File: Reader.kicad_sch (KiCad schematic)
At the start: 39 parts, among them J1 Conn_01x04, J2 Amphenol Dubox ‎76383-402LF‎, J3 Conn_01x04, J4 Conn_01x08, J5 Conn_01x10, J6 Conn_01x03, J7 Conn_01x02, Q1 2N7002, Q2 2N7002, Q3 2N7002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

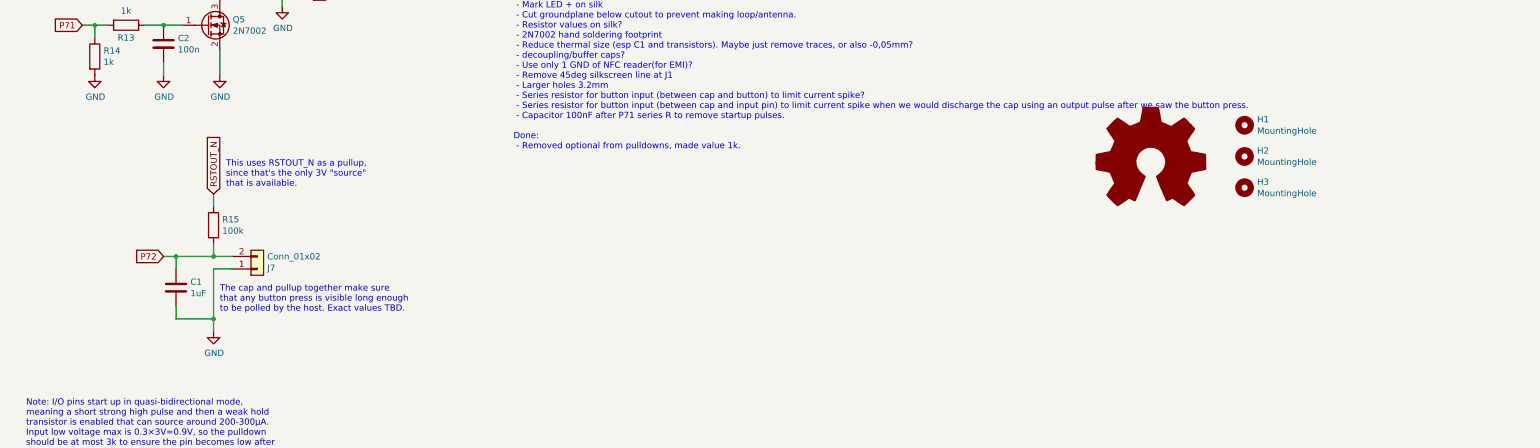
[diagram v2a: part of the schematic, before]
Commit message: Add series resistors for button input
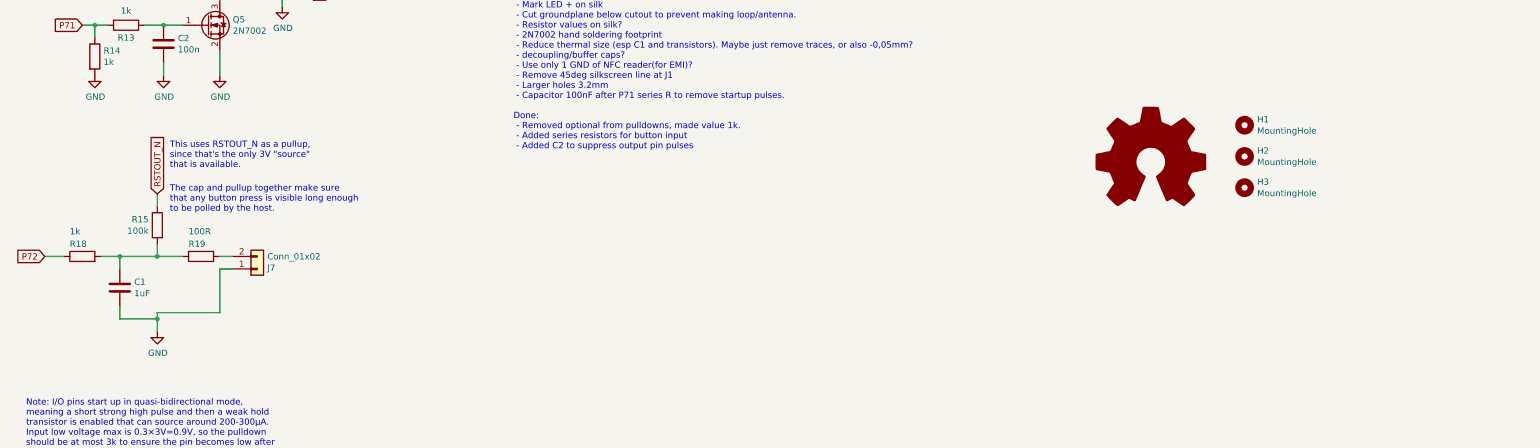
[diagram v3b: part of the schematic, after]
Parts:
- added R18: 1k, Resistor_SMD:R_0805_2012Metric_Pad1.20x1.40mm_HandSolder, symbol Device:R
- added R19: 100R, Resistor_SMD:R_0805_2012Metric_Pad1.20x1.40mm_HandSolder, symbol Device:R
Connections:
- net P72: now also R18.1; no longer C1.1, J7.2 (Pin_2), R15.2
- new net: J7.2 (Pin_2), R19.2
- new net: C1.1, R15.2, R18.2, R19.1
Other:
- note added: "TODO: - Mark LED + on silk - Cut groundplane below cutout to prevent making loop/antenna. - Resistor values on silk? - 2N7002 hand soldering footprint - Reduce thermal size (esp C1 and transistors). Maybe just remove traces, or also -0,05mm? - decoupling/buffer caps? - Use only 1 GND of NFC reader(for EMI)? - Remove 45deg silkscreen line at J1 - Larger holes 3.2mm - Capacitor 100nF after P71 seri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"
- note added: "The cap and pullup together make sure that any button press is visible long enough to be polled by the host."
- note removed: "TODO: - Mark LED + on silk - Cut groundplane below cutout to prevent making loop/antenna. - Resistor values on silk? - 2N7002 hand soldering footprint - Reduce thermal size (esp C1 and transistors). Maybe just remove traces, or also -0,05mm? - decoupling/buffer caps? - Use only 1 GND of NFC reader(for EMI)? - Remove 45deg silkscreen line at J1 - Larger holes 3.2mm - Series resistor for button inp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"
- note removed: "The cap and pullup together make sure that any button press is visible long enough to be polled by the host. Exact values TBD."
- moved on the sheet: C1, R15
